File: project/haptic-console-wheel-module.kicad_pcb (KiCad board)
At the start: 2 copper layers, 68 x 58 mm, 13 parts, among them J1 XH2.54-6P Console, J2 E38S6G5-600B-G24N AB, U1 RaspberryPi_Pico

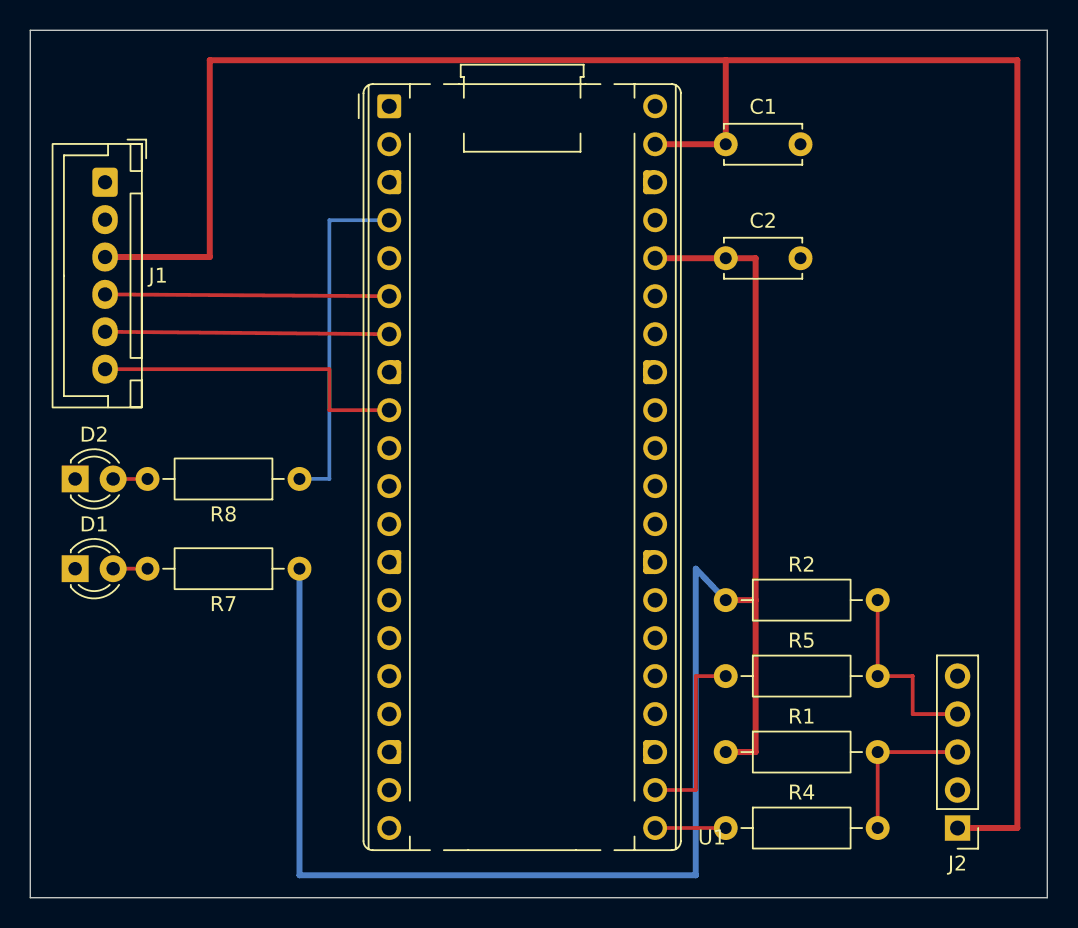
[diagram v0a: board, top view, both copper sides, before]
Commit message: Wheel Module (M3): GND pour, board fully connected (0 DRC errors)
Adds a filled GND zone on B.Cu (3270 mm2 of copper on a 68 x 58 mm board).
All 14 GND pads are through-hole and tie straight into the plane, so GND
needs no routed traces at all.

DRC is now clean: 0 errors, 0 shorts and - importantly - 0 unconnected
items. Every net is connected. The 6 remaining warnings are cosmetic: five
lib_footprint_mismatch (footprint copies written by the placement tool differ
cosmetically from the stock library) and one silk_over_copper on U1's
reference text.

Tooling note: the zone had to be built through pcbnew rather than the MCP
pcb_add_zone tool. That tool returned a UUID but produced no zone pcbnew
could see, and rewriting the file dropped every routed segment. pcbnew's
ZONE.AddPolygon also only accepts a SHAPE_LINE_CHAIN here, not a list of
VECTOR2I, despite both being in the advertised prototypes.

Co-Authored-By: Claude Opus 5 <noreply@anthropic.com>
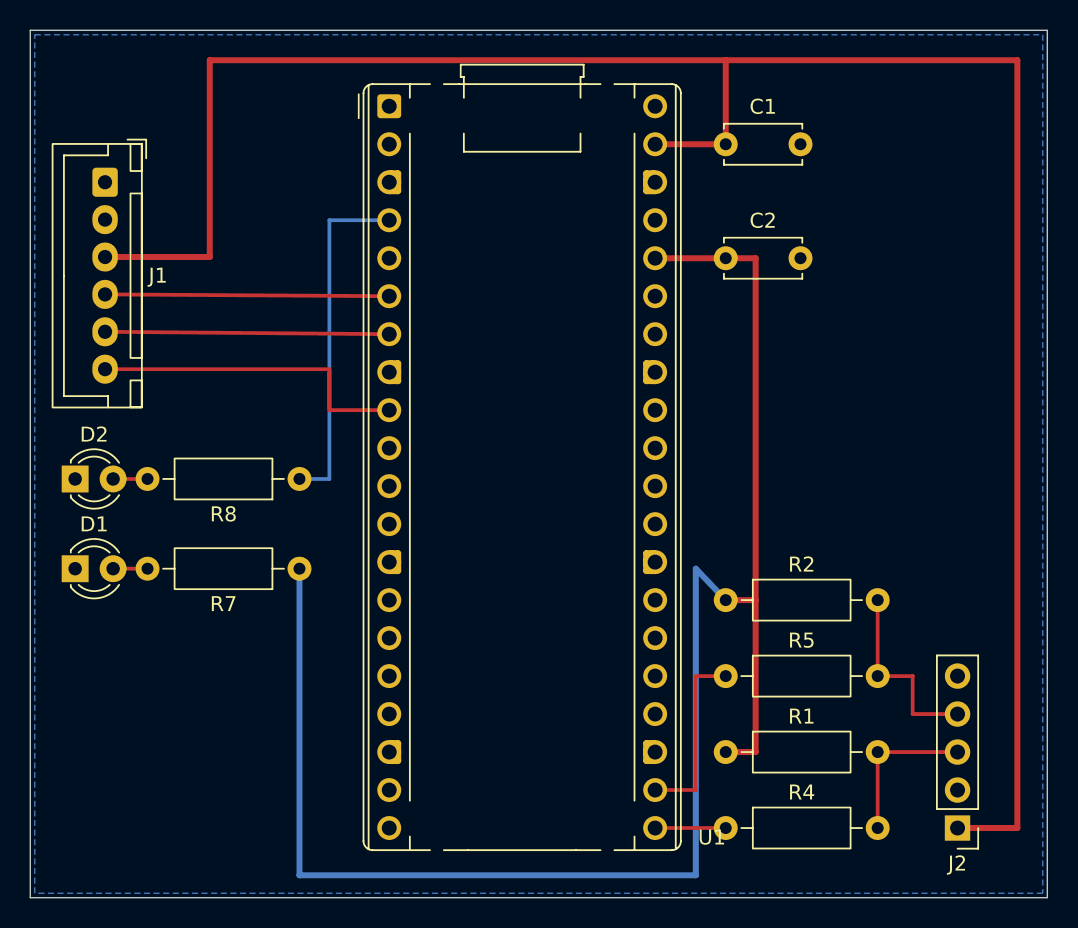
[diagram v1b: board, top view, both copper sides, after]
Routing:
- added copper zone on B.Cu, net GND
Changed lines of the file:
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@@
 		(net "/ENC_B_RAW")
+	)
+	(zone
+		(net "GND")
+		(layer "B.Cu")
+		(hatch edge 0.5)
+		(connect_pads
+			(clearance 0.508)
+		)
+		(min_thickness 0.25)
+		(fill yes
+			(thermal_gap 0.5)
+			(thermal_bridge_width 0.5)
+			(island_removal_mode 0)
+		)
+		(polygon
+			(pts
+				(xy 0.3 0.3) (xy 67.7 0.3) (xy 67.7 57.7) (xy 0.3 57.7)
+			)
+		)
 	)
 	(embedded_fonts no)

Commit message: Wheel Module (M3): C1 becomes a polarised 10uF 25V electrolytic
The owner's actual part is a D4x7 aluminium electrolytic, not the ceramic disc
the first revision specified. Bulk capacitance is what electrolytics are for,
so this is the right part rather than a substitution -- the ceramic was only
ever chosen to dodge a tooling bug (see below).

Schematic: C1 is now Device:C_Polarized with a Voltage field of 25V. Pin 1 was
already +5V and pin 2 GND on all three boards, which is exactly the polarised
convention, so nothing needed rotating or re-netting. ERC 0 violations; the
netlist is unchanged apart from C1's footprint -- 13 components, 39 nets, zero
net-membership differences.

New project-local footprint, libraries/wheel-module.pretty (the first vendored
part here), registered in project/fp-lib-table. No stock CP_Radial pairs a 4 mm
can with a 2.50 mm pitch, and 2.50 is the only pitch that keeps pads on the
2.54 mm grid: 2.00 would sit 0.54 mm off a hole against 0.04 mm for 2.50. It is
generated from the stock D4.0mm_P2.00mm part, not hand-written.

Drawing the real body mattered. Modelled first with the stock 5 mm can as a
stand-in, C1's courtyard overlapped U1 by 0.32 mm and swallowed the col-19 hole
where the +5V link lands, so the engine skipped that via and orphaned the link.
That had pushed C1 three holes right -- a layout change made entirely to
accommodate a part 1 mm bigger than the real one. The true 4.59 mm courtyard
clears U1 by 0.18 mm and C1 sits back at col 18, beside the Pico's VSYS pin.

All three boards match their pre-change DRC baselines exactly: fabricated 6/0,
perfboard 9/32, stripboard 240 warnings / 0 errors / 0 unconnected. The
stripboard rebuild is reproducible -- identical file size, every differing line
a UUID. Requires the matching kicad-stripboard change (footprint_libs), without
which the place stage cannot load a project-local library.

The HTML guide now derives polarity from the footprint read back off the board
(CP_* -> pad 1 = +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
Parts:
- C1: footprint Capacitor_THT:C_Disc_D5.0mm_W2.5mm_P5.00mm -> CP_Radial_D4.0mm_P2.50mm

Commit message: Wheel Module (M3): R4/R5 go from 220R to 330R
The two GPIO series protection resistors on /ENC_A and /ENC_B change value.
Nothing else moves: same footprint, same pads, same nets, so this is a value
edit on all three boards plus the generated documentation.

Schematic edited with the MCP symbol-property tool, the fabricated board and
the perfboard with pcbnew's SetValue, and the stripboard rebuilt from the
updated perfboard seed (strip audit clean - every segment carries one net).
The HTML wiring guide is regenerated; the Markdown guides and README are
hand-updated to match.

Verified: ERC 0 violations, netlist diff is the two value lines only, DRC
unchanged in kind and count on all three boards (fab 6, perfboard 9 with the
expected 32 unconnected, stripboard 0 errors / 240 dangling warnings). Board
renders are untouched because Value sits on F.Fab, not silkscreen.

Co-Authored-By: Claude Opus 5 <noreply@anthropic.com>
Claude-Session: https://claude.ai/code/session_01We1mXR7hae2R2YWrbpwpdH
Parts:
- R4, R5: value 220R -> 330R
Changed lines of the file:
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@@
 			)
 		)
-		(property "Value" "220R"
+		(property "Value" "330R"
 			(at 5.08 2.37 0)
 			(layer "F.Fab")
@@
 			)
 		)
-		(property "Value" "220R"
+		(property "Value" "330R"
 			(at 5.08 2.37 0)
 			(layer "F.Fab")
